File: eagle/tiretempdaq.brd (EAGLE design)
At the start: 64.4 x 35.5 mm, 19 parts, among them J1 RJ11-6PTH, J2 RJ11-6PTH, J3 RJ11-6PTH, J4 RJ11-6PTH, J5 TERM-BLOCK-P4-3.5OST-TE-3.5-4P, J6 TERM-BLOCK-P4-3.5OST-TE-3.5-4P

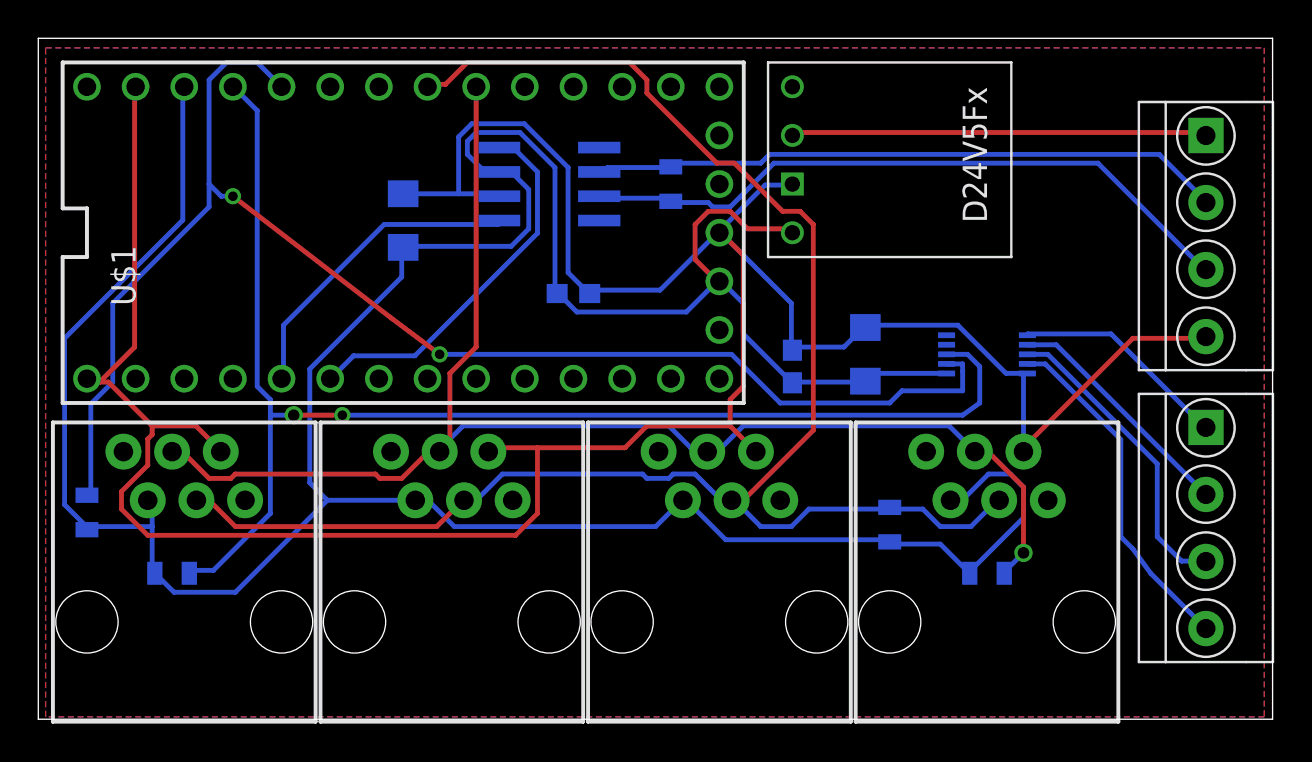
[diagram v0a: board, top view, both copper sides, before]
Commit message: Update board to v0.2 & create v0.1 sensor board
- Re-layout main board to put all analog parts closer together
- Sensor board v0.1
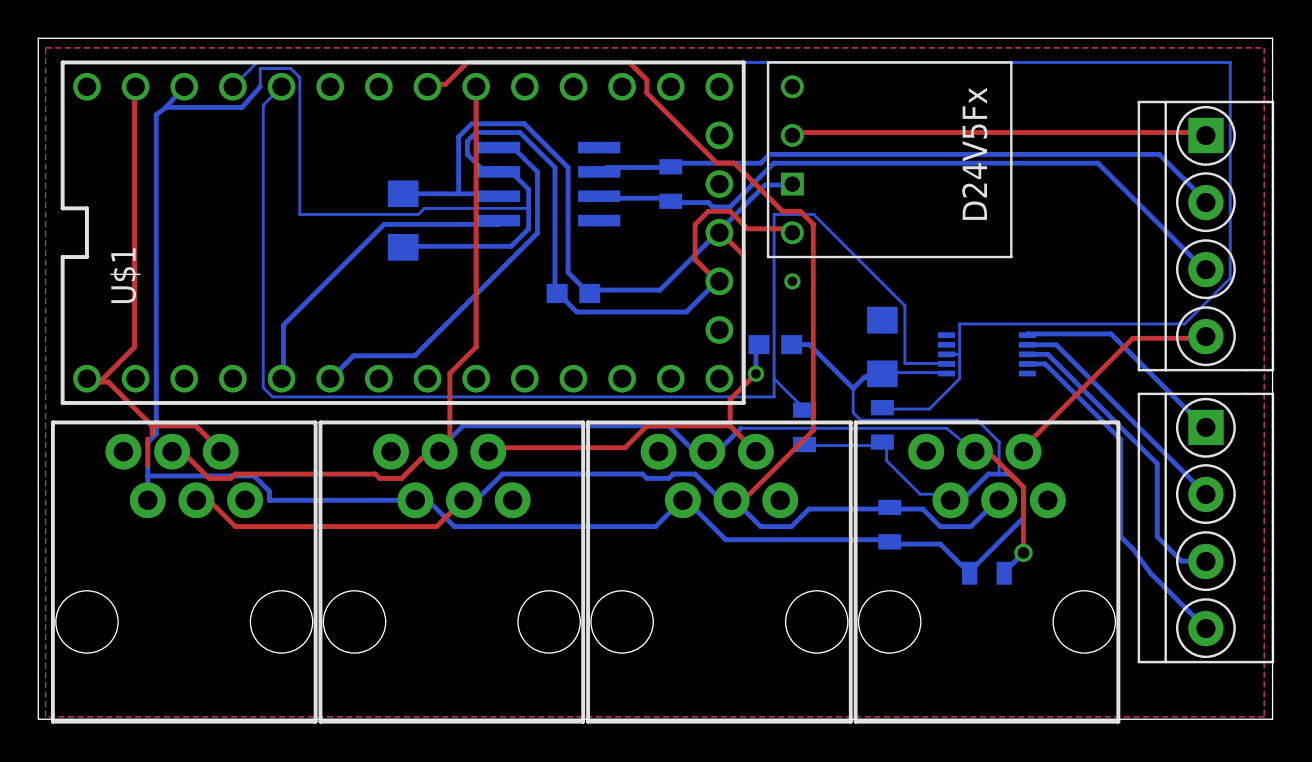
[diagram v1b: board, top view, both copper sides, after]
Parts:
- moved R3 37.9 mm to (44.1, 15.4), turned to 270 degrees
- moved R2 37.7 mm to (40.0, 15.2)
- moved C1 1.45 mm to (38.5, 19.6), turned to 0 degrees
- moved C2 0.97 mm to (44.1, 19.4)
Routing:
- net GND: track 155.7 -> 103.1 mm, vias 0 -> 2
- net DAC_SDA: track 69.8 -> 87.2 mm, vias 2 -> 0
- net 3.3V: track 167.2 -> 182.5 mm
- net DAC_SCL: track 75.0 -> 68.8 mm, vias 2 -> 0
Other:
- board text added: "Analog Out"
- board text added: "S/N:"
- board text added: "TireTempDAQ v0.2 https://synfin.net/tiretempdaq"
- board text removed: "*"
- board text removed: "Analog Out *"
- board text removed: "TireTempDAQ v0.1 https://synfin.net/tiretempdaq"
